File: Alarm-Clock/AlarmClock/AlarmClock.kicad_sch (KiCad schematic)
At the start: 34 parts, among them J1 Jack-DC, J2 output, J3 ISP, SW1 SW_Set, SW2 SW_Inc, SW3 SW_Dec, U1 ATmega8A-A, U2 LM7805_TO220, U5 CC56-12GWA, Y1 Crystal

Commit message: Fixing bugs
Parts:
- removed U2: LM7805_TO220, Package_TO_SOT_THT:TO-220-3_Vertical, symbol Regulator_Linear:LM7805_TO220
- added C6, C7: 18pF, Capacitor_SMD:C_0603_1608Metric, symbol Device:C
- added U2: L7805, Package_TO_SOT_THT:TO-220-3_Horizontal_TabDown, symbol Regulator_Linear:L7805
- D2: footprint Diode_THT:D_DO-35_SOD27_P7.62mm_Horizontal -> Diode_SMD:D_SMA
- Y1: value Crystal -> 32K768
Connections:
- net +12C: now also U2.1 (IN)
- net +5C: now also U2.3 (OUT)
- net GND: now also C6.1, C7.1, U2.2 (GND)
- net MOSI: no longer C5.1, R6.2
- net at C3.1, R1.2: now also U1.22 (ADC7); no longer U1.13 (PB1)
- net at C4.1, R4.2: now also U1.13 (PB1); no longer U1.14 (PB2)
- net at U1.7 (PB6/XTAL1), Y1.2: now also C6.2
- net at U1.8 (PB7/XTAL2), Y1.1: now also C7.2
- new net: C5.1, R6.2, U1.14 (PB2)
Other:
- moved on the sheet: C3, D2, D3, J1, R1, R2, R7, SW1

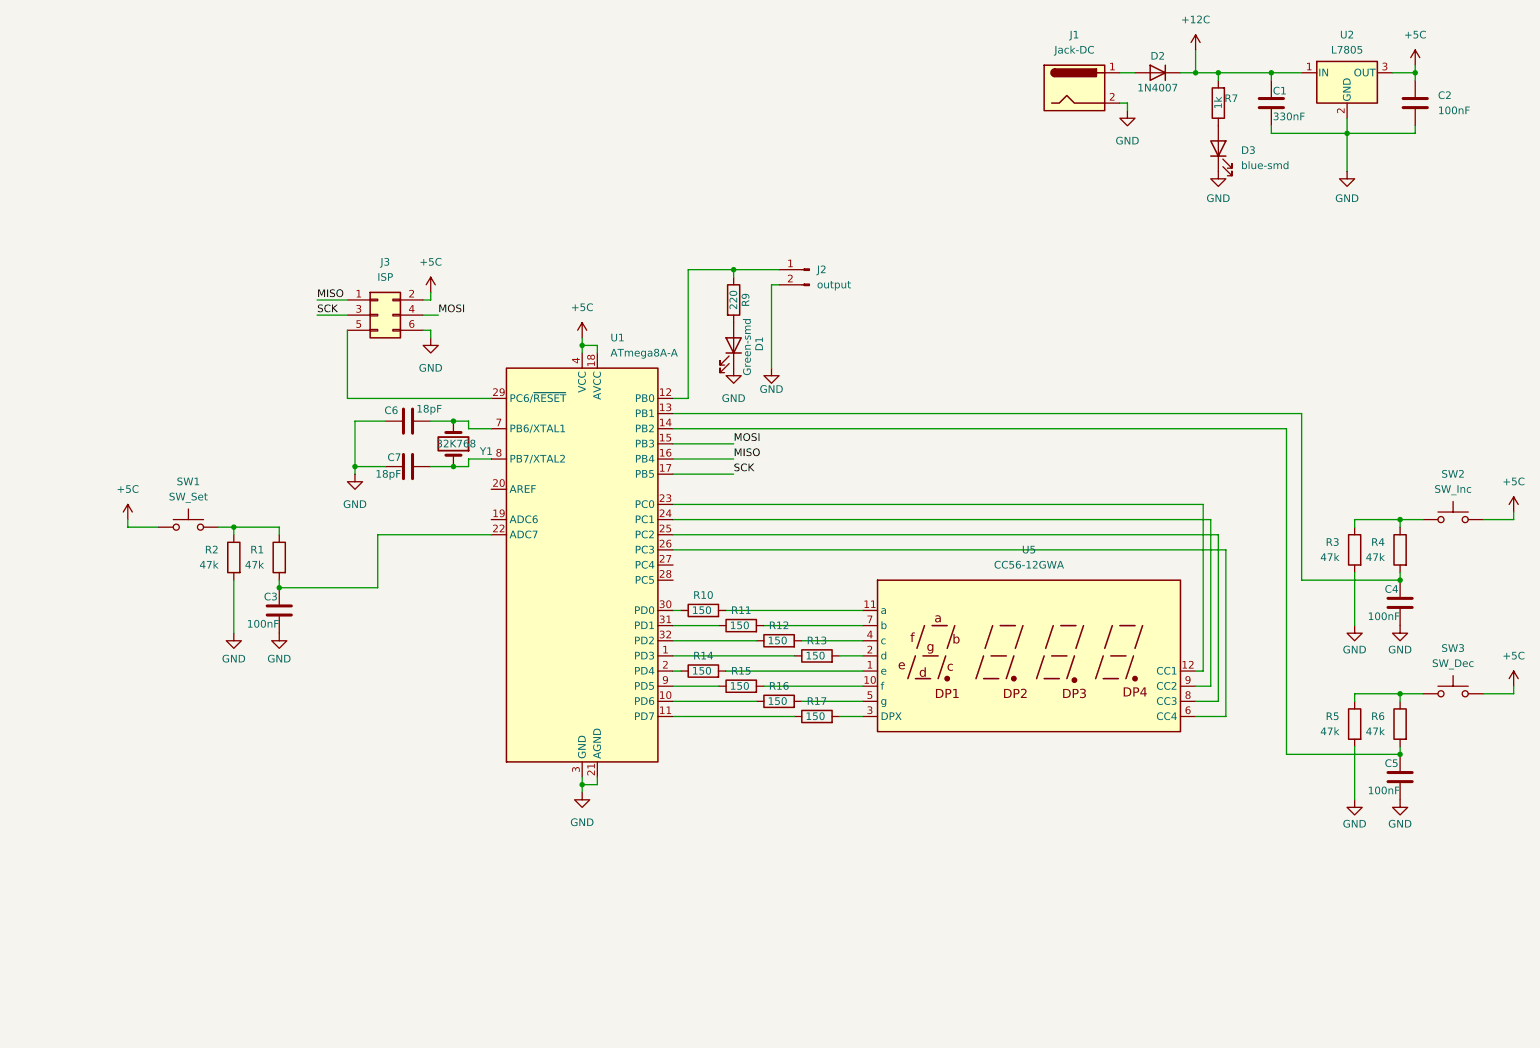
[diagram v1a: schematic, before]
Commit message: Updating/Improving PCB. Adding ground plane, making crystal SMD, some alignments and cleanups. Adding missing crystal capacitors.
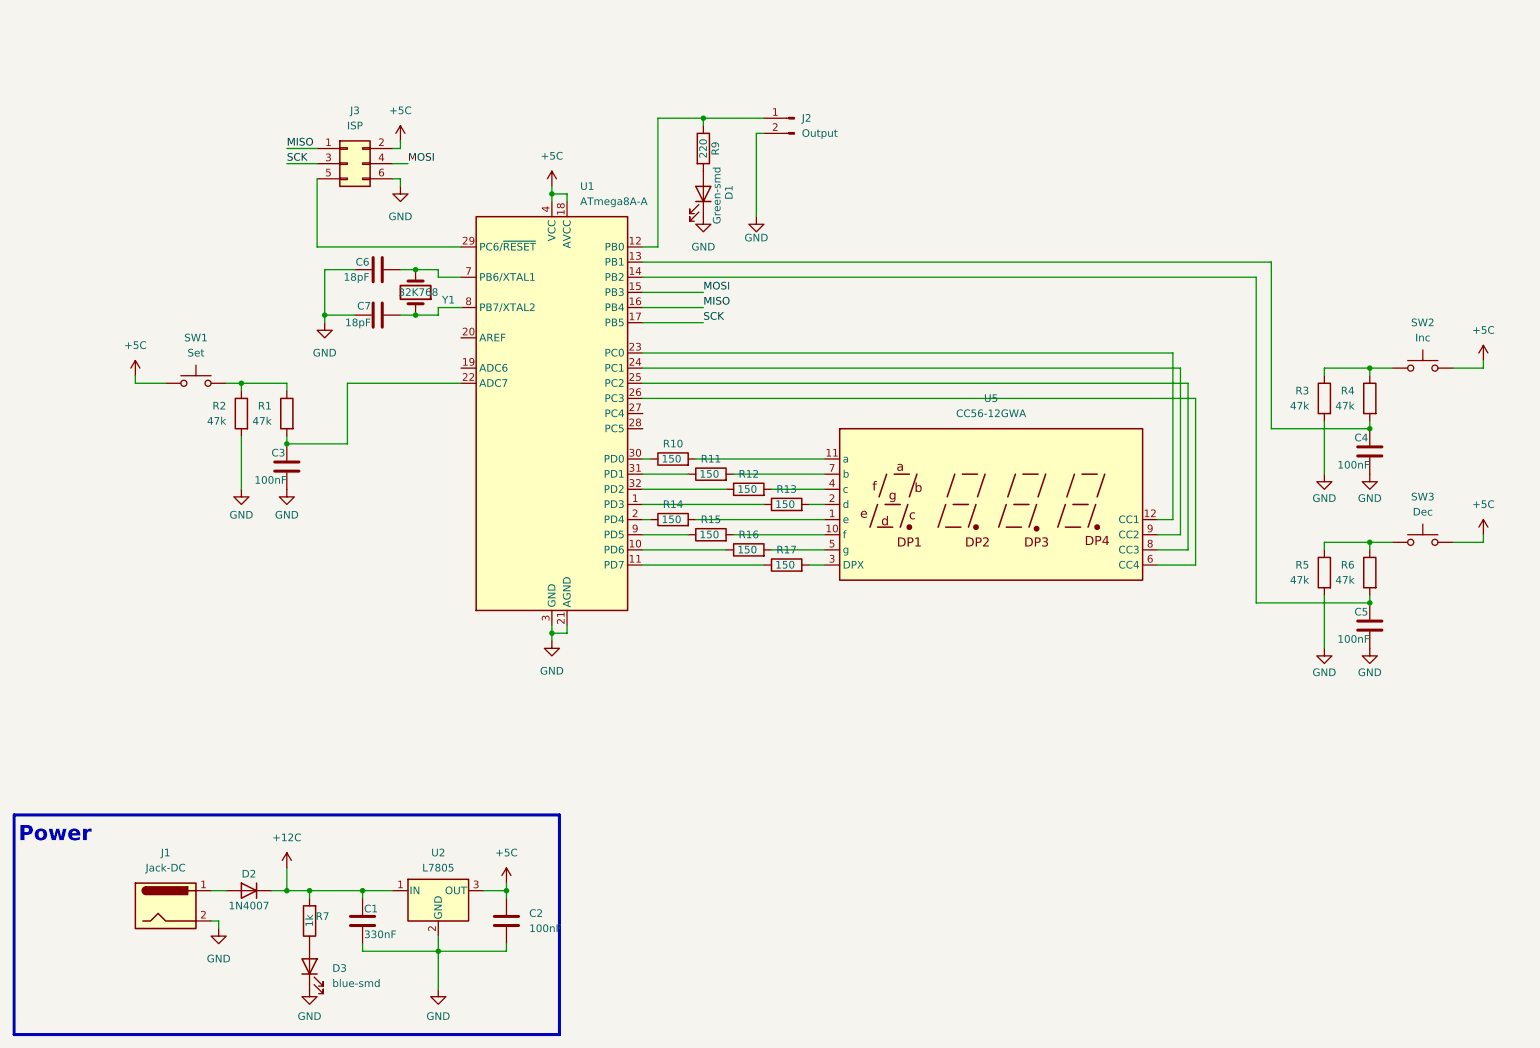
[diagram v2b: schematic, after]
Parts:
- J2: value output -> Output; footprint Connector_Phoenix_MC_HighVoltage:PhoenixContact_MCV_1,5_2-G-5.08_1x02_P5.08mm_Vertical -> Connector_Molex:Molex_KK-254_AE-6410-02A_1x02_P2.54mm_Vertical
- SW1: value SW_Set -> Set
- SW2: value SW_Inc -> Inc
- SW3: value SW_Dec -> Dec
- Y1: footprint Crystal:Crystal_Round_D1.0mm_Vertical -> Crystal:Crystal_SMD_2012-2Pin_2.0x1.2mm
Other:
- note added: "Power"
- moved on the sheet: C1, C2, C3, C4, C5, C6, C7, D1, D2, D3, J1, J2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
